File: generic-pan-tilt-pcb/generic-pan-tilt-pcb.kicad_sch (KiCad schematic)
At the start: 25 parts, among them J1 Conn_01x03, J10 USB_C_Receptacle_USB2.0_14P, J2 NC5MAV, J3 NC5FAV, J4 Conn_01x03, J5 Conn_01x03, J6 Conn_01x03, J7 Conn_01x03, J8 Conn_01x12, J9 Conn_01x12, SW1 SW_Push, SW2 SW_Push

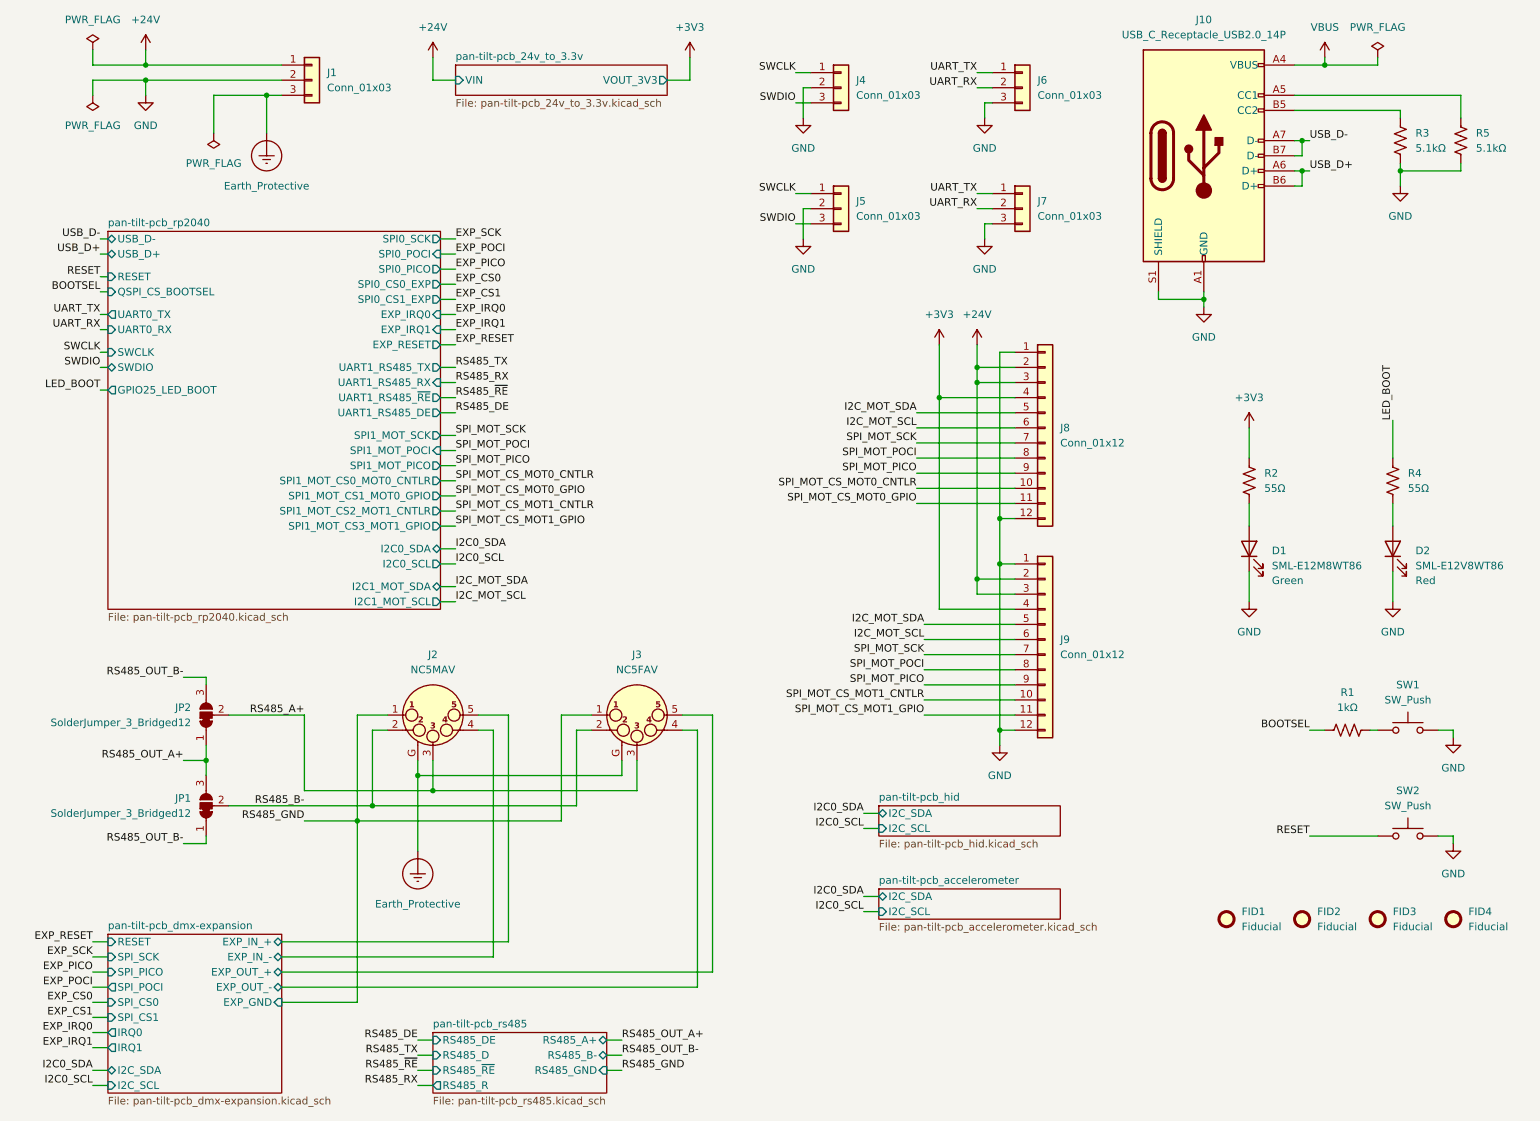
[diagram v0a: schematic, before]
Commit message: rename again to generic-pan-tilt
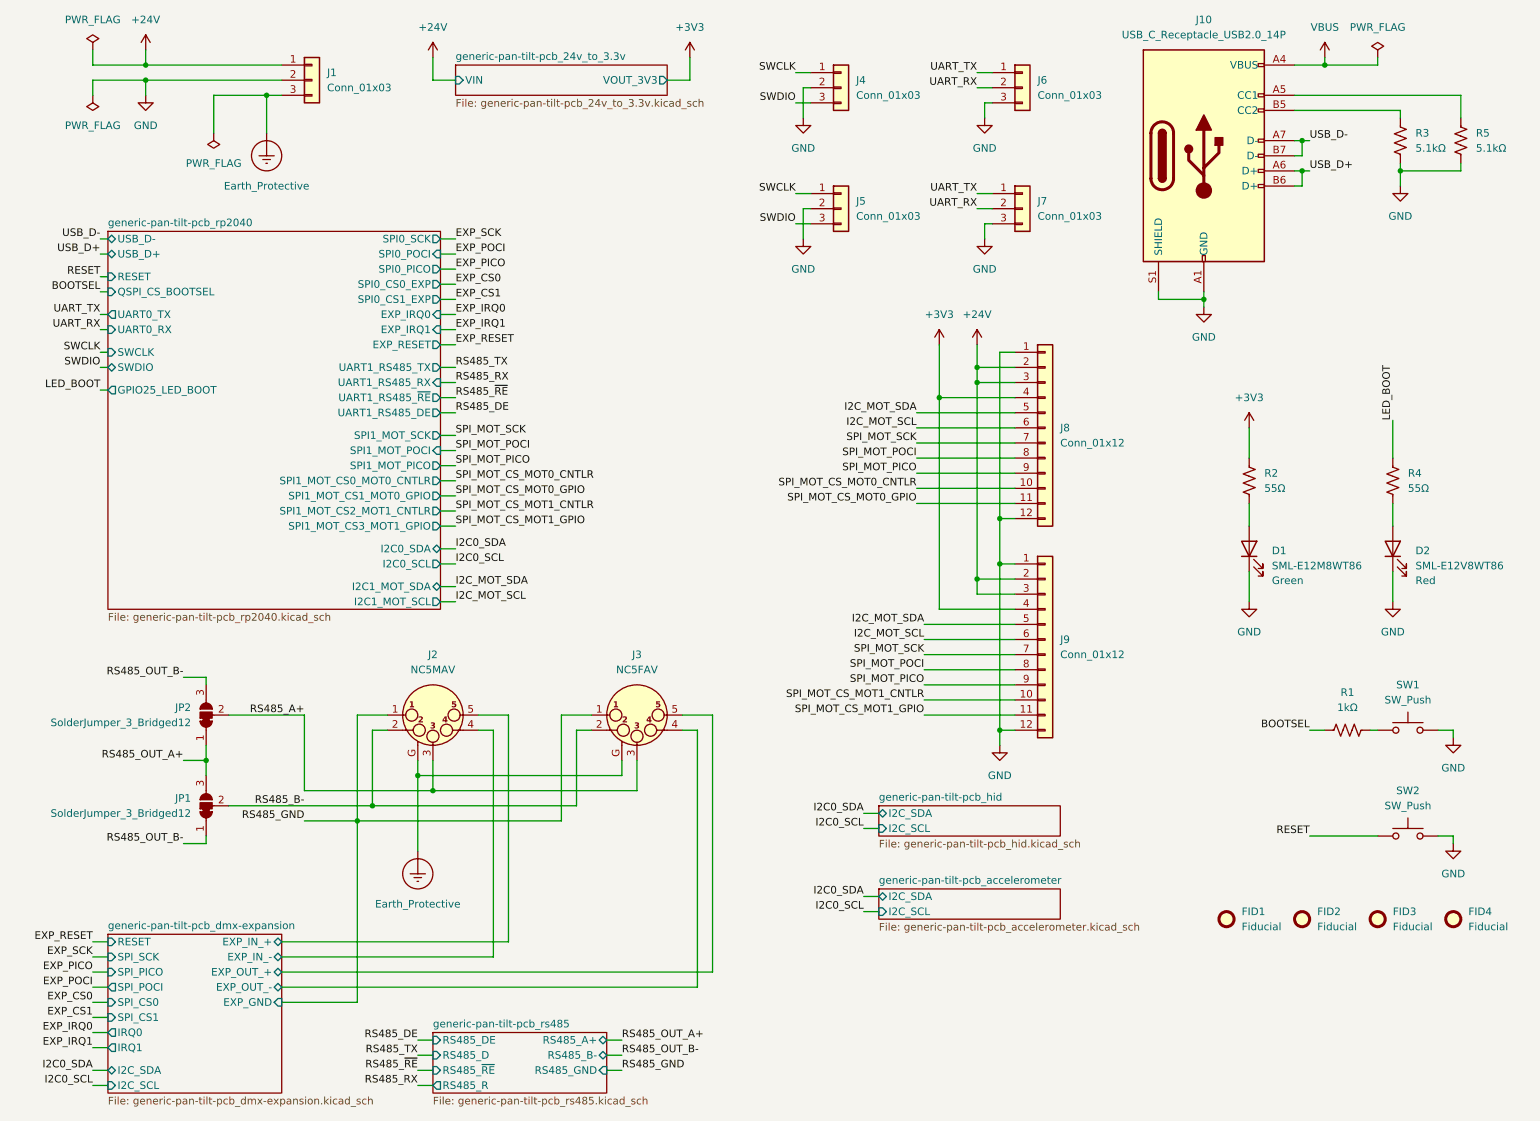
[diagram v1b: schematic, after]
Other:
- sheet pan-tilt-pcb_24v_to_3.3v renamed generic-pan-tilt-pcb_24v_to_3.3v
- sheet pan-tilt-pcb_accelerometer renamed generic-pan-tilt-pcb_accelerometer
- sheet pan-tilt-pcb_dmx-expansion renamed generic-pan-tilt-pcb_dmx-expansion
- sheet pan-tilt-pcb_hid renamed generic-pan-tilt-pcb_hid
- sheet pan-tilt-pcb_rp2040 renamed generic-pan-tilt-pcb_rp2040
- sheet pan-tilt-pcb_rs485 renamed generic-pan-tilt-pcb_rs485
- sheet generic-pan-tilt-pcb_24v_to_3.3v: file pan-tilt-pcb_24v_to_3.3v.kicad_sch -> generic-pan-tilt-pcb_24v_to_3.3v.kicad_sch
- sheet generic-pan-tilt-pcb_accelerometer: file pan-tilt-pcb_accelerometer.kicad_sch -> generic-pan-tilt-pcb_accelerometer.kicad_sch
- sheet generic-pan-tilt-pcb_dmx-expansion: file pan-tilt-pcb_dmx-expansion.kicad_sch -> generic-pan-tilt-pcb_dmx-expansion.kicad_sch
- sheet generic-pan-tilt-pcb_hid: file pan-tilt-pcb_hid.kicad_sch -> generic-pan-tilt-pcb_hid.kicad_sch
- sheet generic-pan-tilt-pcb_rp2040: file pan-tilt-pcb_rp2040.kicad_sch -> generic-pan-tilt-pcb_rp2040.kicad_sch
- sheet generic-pan-tilt-pcb_rs485: file pan-tilt-pcb_rs485.kicad_sch -> generic-pan-tilt-pcb_rs485.kicad_sch
- title: Pan Tilt PCB -> Generic Pan Tilt PCB
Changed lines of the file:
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@@
 	(paper "USLetter")
 	(title_block
-		(title "Pan Tilt PCB")
+		(title "Generic Pan Tilt PCB")
 		(date "2024-07-10")
 		(company "Responsive Environments, MIT Media Lab")
@@
 		)
 		(instances
-			(project "pan-tilt-pcb"
+			(project "generic-pan-tilt-pcb"
 				(path "/e3bbbe58-bf8f-42a8-8505-028de8235dc1"
 					(reference "#PWR020")
@@
 		)
 		(instances
-			(project "pan-tilt-pcb"
+			(project "generic-pan-tilt-pcb"
 				(path "/e3bbbe58-bf8f-42a8-8505-028de8235dc1"
 					(reference "#PWR08")
@@
 		)
 		(instances
-			(project "pan-tilt-pcb"
+			(project "generic-pan-tilt-pcb"
 				(path "/e3bbbe58-bf8f-42a8-8505-028de8235dc1"
 					(reference "R4")
@@
 		)
 		(instances
-			(project "pan-tilt-pcb"
+			(project "generic-pan-tilt-pcb"
 				(path "/e3bbbe58-bf8f-42a8-8505-028de8235dc1"
 					(reference "J4")
@@
 		)
 		(instances
-			(project "pan-tilt-pcb"
+			(project "generic-pan-tilt-pcb"
 				(path "/e3bbbe58-bf8f-42a8-8505-028de8235dc1"
 					(reference "#FLG01")
@@
 		)
 		(instances
-			(project "pan-tilt-pcb"
+			(project "generic-pan-tilt-pcb"
 				(path "/e3bbbe58-bf8f-42a8-8505-028de8235dc1"
 					(reference "#FLG03")
@@
 		)
 		(instances
-			(project "pan-tilt-pcb"
+			(project "generic-pan-tilt-pcb"
 				(path "/e3bbbe58-bf8f-42a8-8505-028de8235dc1"
 					(reference "#PWR013")
@@
 		)
 		(instances
-			(project "pan-tilt-pcb"
+			(project "generic-pan-tilt-pcb"
 				(path "/e3bbbe58-bf8f-42a8-8505-028de8235dc1"
 					(reference "D2")
@@
 		)
 		(instances
-			(project "pan-tilt-pcb"
+			(project "generic-pan-tilt-pcb"
 				(path "/e3bbbe58-bf8f-42a8-8505-028de8235dc1"
 					(reference "#PWR07")
@@
 		)
 		(instances
-			(project "pan-tilt-pcb"
+			(project "generic-pan-tilt-pcb"
 				(path "/e3bbbe58-bf8f-42a8-8505-028de8235dc1"
 					(reference "J7")
@@
 		)
 		(instances
-			(project "pan-tilt-pcb"
+			(project "generic-pan-tilt-pcb"
 				(path "/e3bbbe58-bf8f-42a8-8505-028de8235dc1"
 					(reference "JP2")
@@
 		)
 		(instances
-			(project "pan-tilt-pcb"
+			(project "generic-pan-tilt-pcb"
 				(path "/e3bbbe58-bf8f-42a8-8505-028de8235dc1"
 					(reference "#PWR010")
@@
 		)
 		(instances
-			(project "pan-tilt-pcb"
+			(project "generic-pan-tilt-pcb"
 				(path "/e3bbbe58-bf8f-42a8-8505-028de8235dc1"
 					(reference "J6")
@@
 		)
 		(instances
-			(project "pan-tilt-pcb"
+			(project "generic-pan-tilt-pcb"
 				(path "/e3bbbe58-bf8f-42a8-8505-028de8235dc1"
 					(reference "#PWR09")
@@
 		)
 		(instances
-			(project "pan-tilt-pcb"
+			(project "generic-pan-tilt-pcb"
 				(path "/e3bbbe58-bf8f-42a8-8505-028de8235dc1"
 					(reference "#PWR019")
@@
 		)
 		(instances
-			(project "pan-tilt-pcb"
+			(project "generic-pan-tilt-pcb"
 				(path "/e3bbbe58-bf8f-42a8-8505-028de8235dc1"
 					(reference "R1")
@@
 		)
 		(instances
-			(project "pan-tilt-pcb"
+			(project "generic-pan-tilt-pcb"
 				(path "/e3bbbe58-bf8f-42a8-8505-028de8235dc1"
 					(reference "J9")
@@
 		)
 		(instances
-			(project "pan-tilt-pcb"
+			(project "generic-pan-tilt-pcb"
 				(path "/e3bbbe58-bf8f-42a8-8505-028de8235dc1"
 					(reference "#PWR05")
@@
 		)
 		(instances
-			(project "pan-tilt-pcb"
+			(project "generic-pan-tilt-pcb"
 				(path "/e3bbbe58-bf8f-42a8-8505-028de8235dc1"
 					(reference "SW2")
@@
 		)
 		(instances
-			(project "pan-tilt-pcb"
+			(project "generic-pan-tilt-pcb"
 				(path "/e3bbbe58-bf8f-42a8-8505-028de8235dc1"
 					(reference "SW1")
@@
 		)
 		(instances
-			(project "pan-tilt-pcb"
+			(project "generic-pan-tilt-pcb"
 				(path "/e3bbbe58-bf8f-42a8-8505-028de8235dc1"
 					(reference "#PWR012")
@@
 		)
 		(instances
-			(project "pan-tilt-pcb"
+			(project "generic-pan-tilt-pcb"
 				(path "/e3bbbe58-bf8f-42a8-8505-028de8235dc1"
 					(reference "#PWR021")
@@
 		)
 		(instances
-			(project "pan-tilt-pcb"
+			(project "generic-pan-tilt-pcb"
 				(path "/e3bbbe58-bf8f-42a8-8505-028de8235dc1"
 					(reference "#PWR03")
@@
 		)
 		(instances
-			(project "pan-tilt-pcb"
+			(project "generic-pan-tilt-pcb"
 				(path "/e3bbbe58-bf8f-42a8-8505-028de8235dc1"
 					(reference "#PWR011")
@@
 			(color 0 0 0 0.0000)
 		)
-		(property "Sheetname" "pan-tilt-pcb_rp2040"
+		(property "Sheetname" "generic-pan-tilt-pcb_rp2040"
 			(at 29.21 50.0884 0)
 			(effects
@@
 			)
 		)
-		(property "Sheetfile" "pan-tilt-pcb_rp2040.kicad_sch"
+		(property "Sheetfile" "generic-pan-tilt-pcb_rp2040.kicad_sch"
 			(at 29.21 114.8846 0)
 			(effects
@@
 		)
 		(instances
-			(project "pan-tilt-pcb"
+			(project "generic-pan-tilt-pcb"
 				(path "/e3bbbe58-bf8f-42a8-8505-028de8235dc1"
 					(page "2")
@@
 			(color 0 0 0 0.0000)
 		)
-		(property "Sheetname" "pan-tilt-pcb_hid"
+		(property "Sheetname" "generic-pan-tilt-pcb_hid"
 			(at 158.75 146.6084 0)
 			(effects
@@
 			)
 		)
-		(property "Sheetfile" "pan-tilt-pcb_hid.kicad_sch"
+		(property "Sheetfile" "generic-pan-tilt-pcb_hid.kicad_sch"
 			(at 158.75 152.9846 0)
 			(effects
@@
 		)
 		(instances
-			(project "pan-tilt-pcb"
+			(project "generic-pan-tilt-pcb"
 				(path "/e3bbbe58-bf8f-42a8-8505-028de8235dc1"
 					(page "6")
@@
 			(color 0 0 0 0.0000)
 		)
-		(property "Sheetname" "pan-tilt-pcb_accelerometer"
+		(property "Sheetname" "generic-pan-tilt-pcb_accelerometer"
 			(at 158.75 160.5784 0)
 			(effects
@@
 			)
 		)
-		(property "Sheetfile" "pan-tilt-pcb_accelerometer.kicad_sch"
+		(property "Sheetfile" "generic-pan-tilt-pcb_accelerometer.kicad_sch"
 			(at 158.75 166.9546 0)
 			(effects
@@
 		)
 		(instances
-			(project "pan-tilt-pcb"
+			(project "generic-pan-tilt-pcb"
 				(path "/e3bbbe58-bf8f-42a8-8505-028de8235dc1"
 					(page "7")
@@
 			(color 0 0 0 0.0000)
 		)
-		(property "Sheetname" "pan-tilt-pcb_rs485"
+		(property "Sheetname" "generic-pan-tilt-pcb_rs485"
 			(at 83.82 184.7084 0)
 			(effects
@@
 			)
 		)
-		(property "Sheetfile" "pan-tilt-pcb_rs485.kicad_sch"
+		(property "Sheetfile" "generic-pan-tilt-pcb_rs485.kicad_sch"
 			(at 83.82 196.1646 0)
 			(effects
@@
 		)
 		(instances
-			(project "pan-tilt-pcb"
+			(project "generic-pan-tilt-pcb"
 				(path "/e3bbbe58-bf8f-42a8-8505-028de8235dc1"
 					(page "4")
@@
 			(color 0 0 0 0.0000)
 		)
-		(property "Sheetname" "pan-tilt-pcb_24v_to_3.3v"
+		(property "Sheetname" "generic-pan-tilt-pcb_24v_to_3.3v"
 			(at 87.63 22.1484 0)
 			(effects
@@
 			)
 		)
-		(property "Sheetfile" "pan-tilt-pcb_24v_to_3.3v.kicad_sch"
+		(property "Sheetfile" "generic-pan-tilt-pcb_24v_to_3.3v.kicad_sch"
 			(at 87.63 28.5246 0)
 			(effects
@@
 		)
 		(instances
-			(project "pan-tilt-pcb"
+			(project "generic-pan-tilt-pcb"
 				(path "/e3bbbe58-bf8f-42a8-8505-028de8235dc1"
 					(page "3")
@@
 			(color 0 0 0 0.0000)
 		)
-		(property "Sheetname" "pan-tilt-pcb_dmx-expansion"
+		(property "Sheetname" "generic-pan-tilt-pcb_dmx-expansion"
 			(at 29.21 168.1984 0)
 			(effects
@@
 			)
 		)
-		(property "Sheetfile" "pan-tilt-pcb_dmx-expansion.kicad_sch"
+		(property "Sheetfile" "generic-pan-tilt-pcb_dmx-expansion.kicad_sch"
 			(at 29.21 196.1646 0)
 			(effects
@@
 		)
 		(instances
-			(project "pan-tilt-pcb"
+			(project "generic-pan-tilt-pcb"
 				(path "/e3bbbe58-bf8f-42a8-8505-028de8235dc1"
 					(page "5")

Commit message: pick all footprints, begin layout
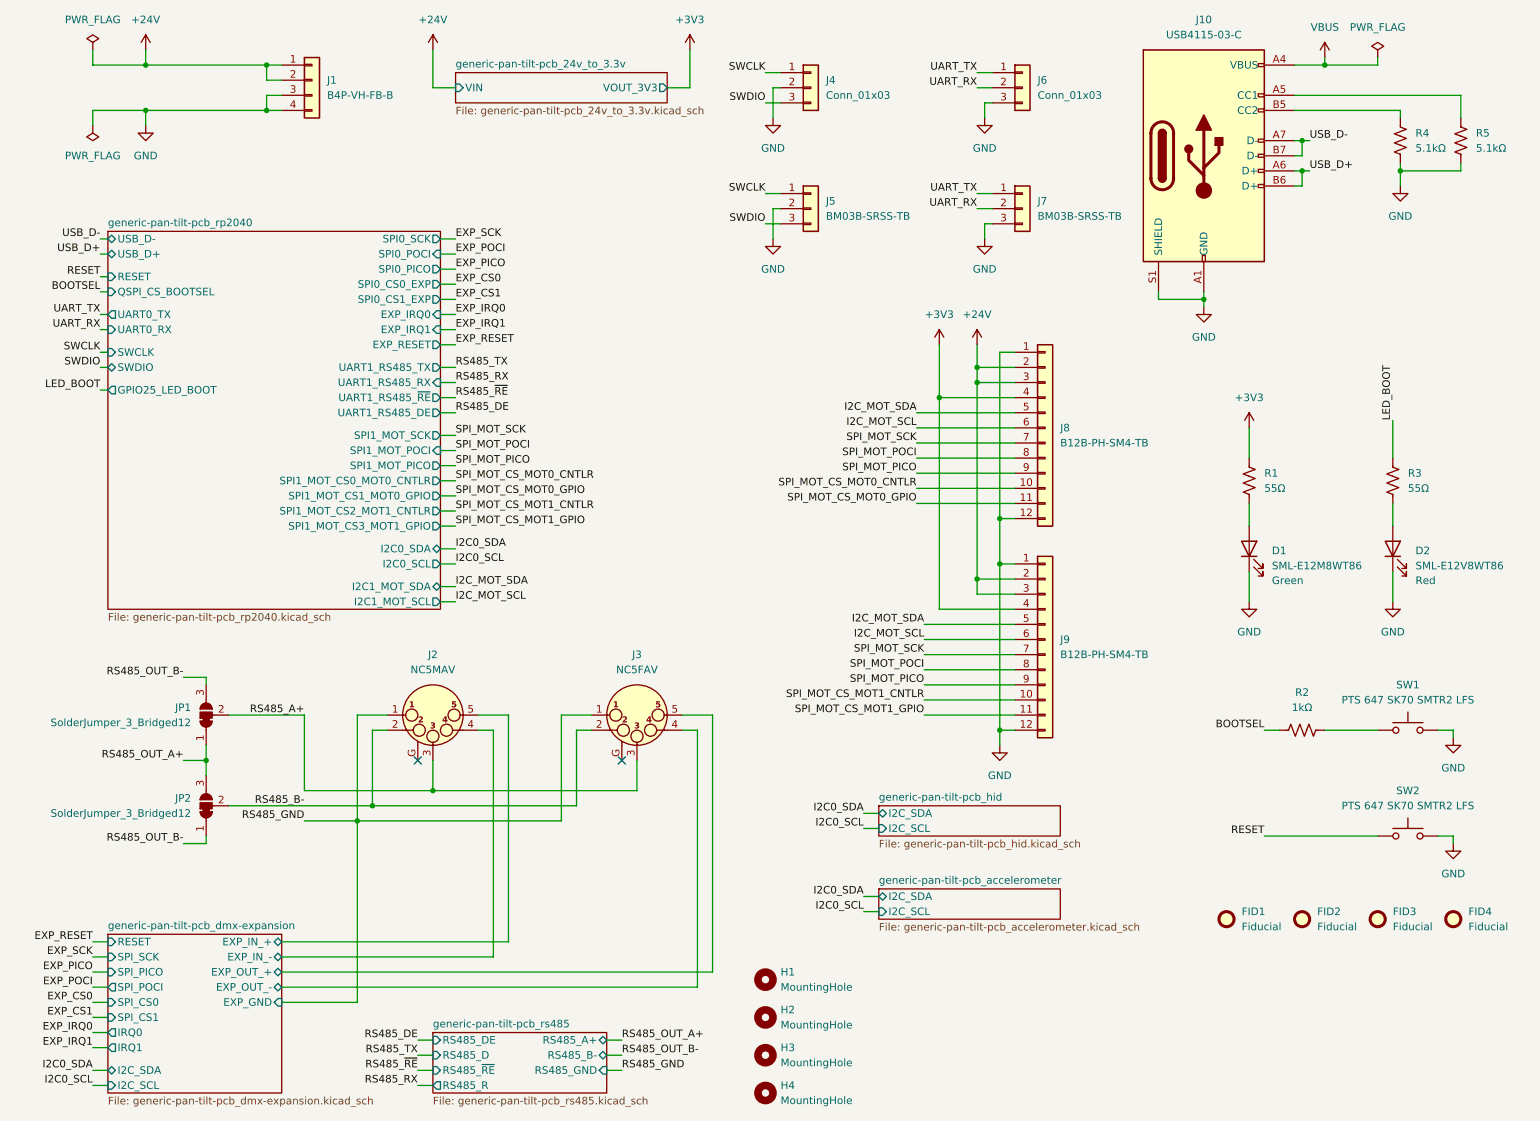
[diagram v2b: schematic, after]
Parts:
- removed J1: Conn_01x03, symbol Connector_Generic:Conn_01x03
- added H1, H2, H3, H4: MountingHole, MountingHole:MountingHole_3.2mm_M3, symbol Mechanical:MountingHole
- added J1: B4P-VH-FB-B, Connector_JST:JST_VH_B4PS-VH_1x04_P3.96mm_Horizontal, symbol Connector_Generic:Conn_01x04
- D2: footprint (none) -> LED_SMD:LED_0603_1608Metric
- FID1, FID2, FID3, FID4: footprint (none) -> Fiducial:Fiducial_0.5mm_Mask1mm
- J10: value USB_C_Receptacle_USB2.0_14P -> USB4115-03-C; footprint (none) -> Connector_USB:USB_C_Receptacle_GCT_USB4115-03-C
- J2: footprint Connector_Audio:Jack_XLR_Neutrik_NC5MAV_Vertical -> generic-pan-tilt-pcb:Jack_XLR_Neutrik_NC5MAV_Vertical_mod
- J3: footprint Connector_Audio:Jack_XLR_Neutrik_NC5FAV_Vertical -> generic-pan-tilt-pcb:Jack_XLR_Neutrik_NC5FAV_Vertical_mod
- J4, J6: footprint (none) -> Connector_PinHeader_2.54mm:PinHeader_1x03_P2.54mm_Vertical_SMD_Pin1Left
- J5, J7: value Conn_01x03 -> BM03B-SRSS-TB; footprint (none) -> Connector_JST:JST_SH_BM03B-SRSS-TB_1x03-1MP_P1.00mm_Vertical
- J8, J9: value Conn_01x12 -> B12B-PH-SM4-TB; footprint (none) -> Connector_JST:JST_PH_B12B-PH-SM4-TB_1x12-1MP_P2.00mm_Vertical
- JP1: renamed from JP2; footprint (none) -> Jumper:SolderJumper-3_P1.3mm_Bridged12_RoundedPad1.0x1.5mm_NumberLabels
- JP2: renamed from JP1; footprint (none) -> Jumper:SolderJumper-3_P1.3mm_Bridged12_RoundedPad1.0x1.5mm_NumberLabels
- R1: renamed from R2; footprint (none) -> Resistor_SMD:R_0603_1608Metric
- R2: renamed from R1; footprint (none) -> Resistor_SMD:R_0603_1608Metric
- R3: renamed from R4; footprint (none) -> Resistor_SMD:R_0603_1608Metric
- R4: renamed from R3; footprint (none) -> Resistor_SMD:R_0603_1608Metric
- R5: footprint (none) -> Resistor_SMD:R_0603_1608Metric
- SW1, SW2: value SW_Push -> PTS 647 SK70 SMTR2 LFS; footprint (none) -> Button_Switch_SMD:SW_SPST_PTS647_Sx70
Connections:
- net +24V: now also J1.1 (Pin_1), J1.2 (Pin_2)
- net GND: now also J1.3 (Pin_3), J1.4 (Pin_4)
- net Earth_Protective: no longer names the net of J3.G
- net Earth_Protective: no longer J2.G
- no-connect marks 0 -> 2
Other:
- moved on the sheet: J4, J5, R2

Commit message: more progress
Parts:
- J4, J6: now not fitted; now left out of the parts list
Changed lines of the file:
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@@
 		(unit 1)
 		(exclude_from_sim no)
-		(in_bom yes)
-		(on_board yes)
-		(dnp no)
+		(in_bom no)
+		(on_board no)
+		(dnp yes)
 		(property "Reference" "J4"
 			(at 149.86 25.3999 0)
@@
 		(unit 1)
 		(exclude_from_sim no)
-		(in_bom yes)
-		(on_board yes)
-		(dnp no)
+		(in_bom no)
+		(on_board no)
+		(dnp yes)
 		(property "Reference" "J6"
 			(at 185.42 25.3999 0)

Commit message: begin new routing
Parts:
- R1, R2, R3, R4, R5: footprint Resistor_SMD:R_0603_1608Metric -> Capacitor_SMD:C_0402_1005Metric
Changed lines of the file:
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@@
 			)
 		)
-		(property "Footprint" "Resistor_SMD:R_0603_1608Metric"
+		(property "Footprint" "Capacitor_SMD:C_0402_1005Metric"
 			(at 246.126 92.964 90)
 			(effects
@@
 			)
 		)
-		(property "Footprint" "Resistor_SMD:R_0603_1608Metric"
+		(property "Footprint" "Capacitor_SMD:C_0402_1005Metric"
 			(at 221.996 92.964 90)
 			(effects
@@
 			)
 		)
-		(property "Footprint" "Resistor_SMD:R_0603_1608Metric"
+		(property "Footprint" "Capacitor_SMD:C_0402_1005Metric"
 			(at 247.396 35.814 90)
 			(effects
@@
 			)
 		)
-		(property "Footprint" "Resistor_SMD:R_0603_1608Metric"
+		(property "Footprint" "Capacitor_SMD:C_0402_1005Metric"
 			(at 230.124 133.604 90)
 			(effects
@@
 			)
 		)
-		(property "Footprint" "Resistor_SMD:R_0603_1608Metric"
+		(property "Footprint" "Capacitor_SMD:C_0402_1005Metric"
 			(at 255.524 35.306 90)
 			(effects
